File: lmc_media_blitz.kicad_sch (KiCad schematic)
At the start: 30 parts, among them J3 Conn_ARM_JTAG_SWD_10, Q1 BSS138, Q2 BSS138, U1 TPS61222DCK, U2 TLV77333PDBVR, U3 LPC804M101JDH20

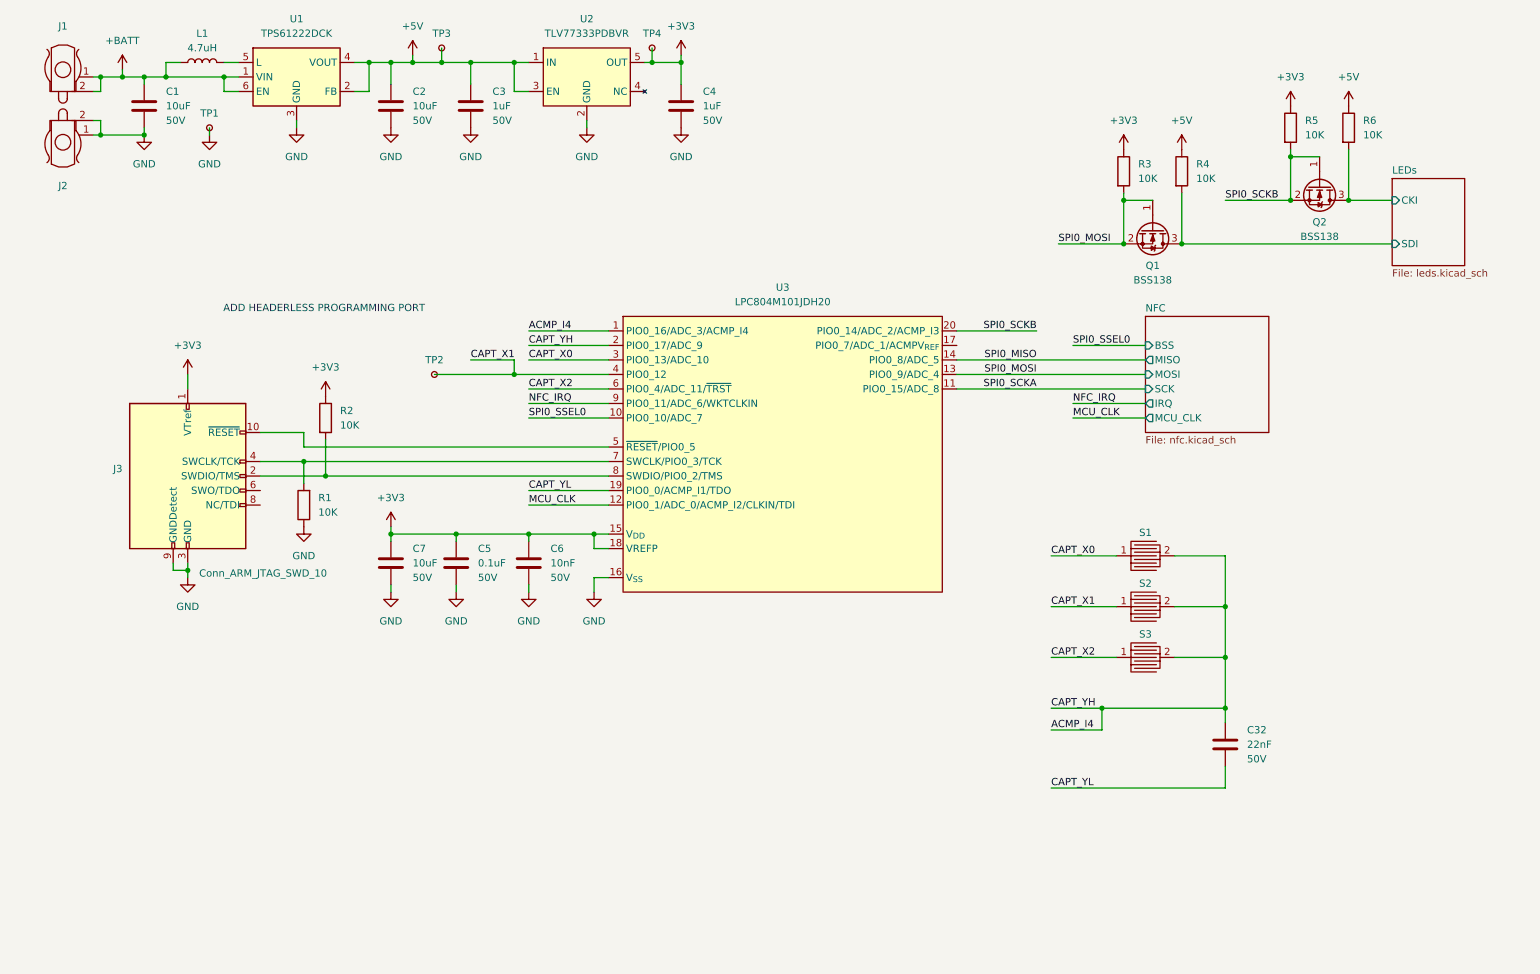
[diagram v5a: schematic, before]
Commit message: Fixed most DRC errors, but need to relayout RFO/RFI
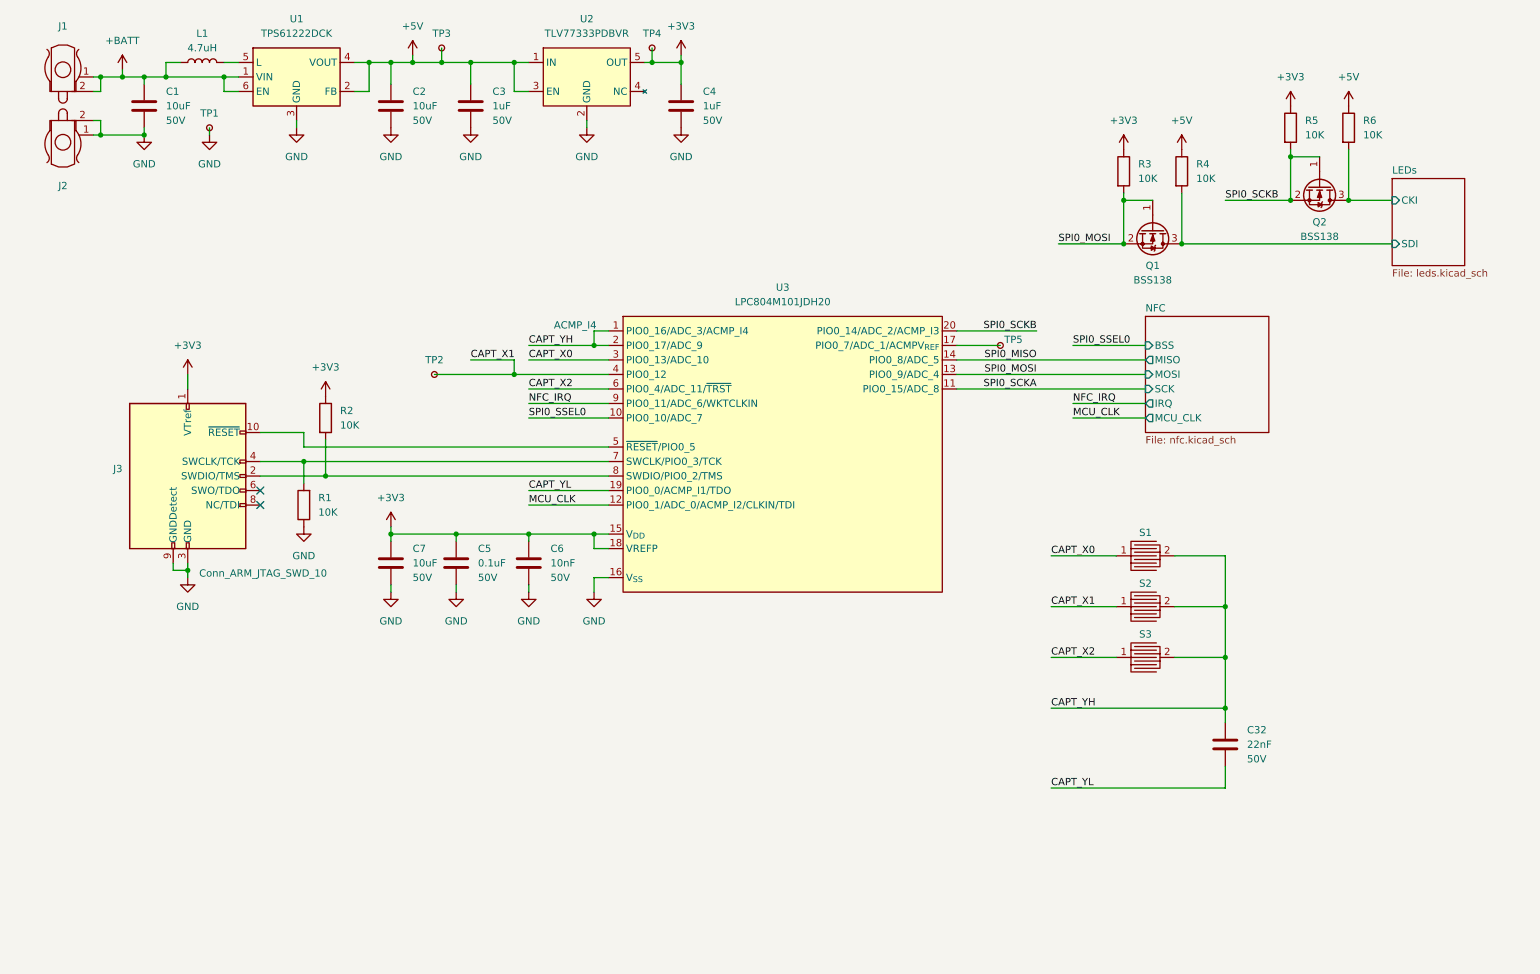
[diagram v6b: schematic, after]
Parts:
- added TP5: TestPoint_Small, TestPoint:TestPoint_Pad_D2.0mm, symbol Connector:TestPoint_Small
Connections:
- net at U3.17 (PIO0_7/ADC_1/ACMPV_{REF}): now also TP5.1
- net ACMP_I4 renamed CAPT_YH
- no-connect marks 0 -> 2
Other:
- note added: "ACMP_I4"
- note removed: "ADD HEADERLESS PROGRAMMING PORT"
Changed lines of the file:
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@@
 	)
 	(junction
-		(at 208.28 52.07)
+		(at 115.57 77.47)
 		(diameter 0)
 		(color 0 0 0 0)
 	)
 	(junction
-		(at 83.82 27.94)
+		(at 208.28 52.07)
 		(diameter 0)
 		(color 0 0 0 0)
 	)
 	(junction
-		(at 237.49 52.07)
+		(at 83.82 27.94)
 		(diameter 0)
 		(color 0 0 0 0)
 	)
 	(junction
-		(at 88.9 27.94)
+		(at 237.49 52.07)
 		(diameter 0)
 		(color 0 0 0 0)
 	)
 	(junction
-		(at 204.47 140.97)
+		(at 88.9 27.94)
 		(diameter 0)
 		(color 0 0 0 0)
@@
 		(color 0 0 0 0)
 	)
+	(no_connect
+		(at 57.15 102.87)
+	)
+	(no_connect
+		(at 57.15 105.41)
+	)
 	(wire
 		(pts
@@
 	(wire
 		(pts
-			(xy 195.58 140.97) (xy 204.47 140.97)
-		)
-		(stroke
-			(width 0)
-			(type default)
-		)
-	)
-	(wire
-		(pts
 			(xy 80.01 27.94) (xy 80.01 31.75)
 		)
@@
 	(wire
 		(pts
-			(xy 104.14 77.47) (xy 118.11 77.47)
+			(xy 104.14 77.47) (xy 115.57 77.47)
 		)
 		(stroke
@@
 	(wire
 		(pts
+			(xy 115.57 74.93) (xy 115.57 77.47)
+		)
+		(stroke
+			(width 0)
+			(type default)
+		)
+	)
+	(wire
+		(pts
 			(xy 91.44 119.38) (xy 91.44 120.65)
 		)
@@
 	(wire
 		(pts
-			(xy 101.6 33.02) (xy 101.6 27.94)
+			(xy 179.07 77.47) (xy 186.69 77.47)
 		)
 		(stroke
@@
 	(wire
 		(pts
-			(xy 104.14 74.93) (xy 118.11 74.93)
+			(xy 101.6 33.02) (xy 101.6 27.94)
 		)
 		(stroke
@@
 	(wire
 		(pts
-			(xy 204.47 144.78) (xy 204.47 140.97)
+			(xy 115.57 77.47) (xy 118.11 77.47)
 		)
 		(stroke
@@
 	(wire
 		(pts
+			(xy 118.11 74.93) (xy 115.57 74.93)
+		)
+		(stroke
+			(width 0)
+			(type default)
+		)
+	)
+	(wire
+		(pts
 			(xy 104.14 85.09) (xy 118.11 85.09)
 		)
@@
 	(wire
 		(pts
-			(xy 195.58 144.78) (xy 204.47 144.78)
-		)
-		(stroke
-			(width 0)
-			(type default)
-		)
-	)
-	(wire
-		(pts
-			(xy 204.47 140.97) (xy 226.06 140.97)
+			(xy 195.58 140.97) (xy 226.06 140.97)
 		)
 		(stroke
@@
 		)
 	)
-	(text "ADD HEADERLESS PROGRAMMING PORT"
+	(text "ACMP_I4"
 		(exclude_from_sim no)
-		(at 68.326 71.12 0)
+		(at 112.268 74.168 0)
 		(effects
 			(font
 				(size 1.27 1.27)
-				(color 255 0 26 1)
 			)
 		)
@@
 		)
 	)
-	(label "ACMP_I4"
-		(at 195.58 144.78 0)
-		(effects
-			(font
-				(size 1.27 1.27)
-			)
-			(justify left bottom)
-		)
-	)
 	(label "CAPT_X2"
 		(at 104.14 85.09 0)
@@
 		)
 	)
-	(label "ACMP_I4"
-		(at 104.14 74.93 0)
-		(effects
-			(font
-				(size 1.27 1.27)
-			)
-			(justify left bottom)
-		)
-	)
 	(label "CAPT_X0"
 		(at 104.14 80.01 0)
@@
 	)
 	(symbol
+		(lib_id "Connector:TestPoint_Small")
+		(at 186.69 77.47 90)
+		(unit 1)
+		(exclude_from_sim no)
+		(in_bom yes)
+		(on_board yes)
+		(dnp no)
+		(property "Reference" "TP5"
+			(at 188.976 76.454 90)
+			(effects
+				(font
+					(size 1.27 1.27)
+				)
+			)
+		)
+		(property "Value" "TestPoint_Small"
+			(at 187.9599 76.2 0)
+			(effects
+				(font
+					(size 1.27 1.27)
+				)
+				(justify left)
+				(hide yes)
+			)
+		)
+		(property "Footprint" "TestPoint:TestPoint_Pad_D2.0mm"
+			(at 186.69 72.39 0)
+			(effects
+				(font
+					(size 1.27 1.27)
+				)
+				(hide yes)
+			)
+		)
+		(property "Datasheet" "~"
+			(at 186.69 72.39 0)
+			(effects
+				(font
+					(size 1.27 1.27)
+				)
+				(hide yes)
+			)
+		)
+		(property "Description" "test point"
+			(at 186.69 77.47 0)
+			(effects
+				(font
+					(size 1.27 1.27)
+				)
+				(hide yes)
+			)
+		)
+		(pin "1"
+		)
+		(instances
+			(project "lmc_media_blitz"
+				(path "/b87eb037-3127-4116-a225-5eb939725614"
+					(reference "TP5")
+					(unit 1)
+				)
+			)
+		)
+	)
+	(symbol
 		(lib_id "Device:R")
 		(at 208.28 46.99 0)
@@
 			)
 		)
-		(property "Datasheet" "https://wmsc.lcsc.com/wmsc/upload/file/pdf/v2/lcsc/2304140030_Taiyo-Yuden-NR3015T4R7M_C87172.pdf"
+		(property "Datasheet" "~"
 			(at 46.99 27.94 0)
 			(effects

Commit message: Added more
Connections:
- net +BATT: now also TP5.1, U3.17 (PIO0_7/ADC_1/ACMPV_{REF})
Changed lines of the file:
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@@
 	)
 	(junction
-		(at 33.02 30.48)
+		(at 35.56 30.48)
 		(diameter 0)
 		(color 0 0 0 0)
@@
 	)
 	(junction
+		(at 31.75 30.48)
+		(diameter 0)
+		(color 0 0 0 0)
+	)
+	(junction
 		(at 208.28 59.69)
 		(diameter 0)
@@
 	(wire
 		(pts
+			(xy 31.75 30.48) (xy 35.56 30.48)
+		)
+		(stroke
+			(width 0)
+			(type default)
+		)
+	)
+	(wire
+		(pts
 			(xy 88.9 25.4) (xy 88.9 27.94)
 		)
@@
 	(wire
 		(pts
+			(xy 36.83 30.48) (xy 40.64 30.48)
+		)
+		(stroke
+			(width 0)
+			(type default)
+		)
+	)
+	(wire
+		(pts
 			(xy 218.44 50.8) (xy 218.44 59.69)
 		)
@@
 	(wire
 		(pts
+			(xy 195.58 71.12) (xy 195.58 77.47)
+		)
+		(stroke
+			(width 0)
+			(type default)
+		)
+	)
+	(wire
+		(pts
 			(xy 195.58 123.19) (xy 207.01 123.19)
 		)
@@
 	(wire
 		(pts
-			(xy 179.07 77.47) (xy 186.69 77.47)
+			(xy 179.07 77.47) (xy 195.58 77.47)
 		)
 		(stroke
@@
 	(wire
 		(pts
-			(xy 33.02 30.48) (xy 33.02 29.21)
+			(xy 31.75 30.48) (xy 31.75 29.21)
 		)
 		(stroke
@@
 	(wire
 		(pts
+			(xy 35.56 27.94) (xy 35.56 30.48)
+		)
+		(stroke
+			(width 0)
+			(type default)
+		)
+	)
+	(wire
+		(pts
 			(xy 115.57 77.47) (xy 118.11 77.47)
 		)
@@
 	(wire
 		(pts
-			(xy 29.21 30.48) (xy 33.02 30.48)
+			(xy 29.21 30.48) (xy 31.75 30.48)
 		)
 		(stroke
@@
 	(wire
 		(pts
-			(xy 36.83 30.48) (xy 33.02 30.48)
+			(xy 36.83 30.48) (xy 35.56 30.48)
 		)
 		(stroke
@@
 	(wire
 		(pts
-			(xy 40.64 30.48) (xy 36.83 30.48)
-		)
-		(stroke
-			(width 0)
-			(type default)
-		)
-	)
-	(wire
-		(pts
 			(xy 44.45 116.84) (xy 44.45 118.11)
 		)
@@
 	(symbol
 		(lib_id "power:+BATT")
-		(at 33.02 29.21 0)
+		(at 31.75 29.21 0)
 		(unit 1)
 		(exclude_from_sim no)
@@
 		(fields_autoplaced yes)
 		(property "Reference" "#PWR04"
-			(at 33.02 33.02 0)
+			(at 31.75 33.02 0)
 			(effects
 				(font
@@
 		)
 		(property "Value" "+BATT"
-			(at 33.02 24.13 0)
+			(at 31.75 24.13 0)
 			(effects
 				(font
@@
 		)
 		(property "Footprint" ""
-			(at 33.02 29.21 0)
+			(at 31.75 29.21 0)
 			(effects
 				(font
@@
 		)
 		(property "Datasheet" ""
-			(at 33.02 29.21 0)
+			(at 31.75 29.21 0)
 			(effects
 				(font
@@
 		)
 		(property "Description" "Power symbol creates a global label with name \"+BATT\""
-			(at 33.02 29.21 0)
+			(at 31.75 29.21 0)
 			(effects
 				(font
@@
 	)
 	(symbol
-		(lib_id "Connector:TestPoint_Small")
-		(at 186.69 77.47 90)
-		(unit 1)
-		(exclude_from_sim no)
-		(in_bom yes)
-		(on_board yes)
-		(dnp no)
-		(property "Reference" "TP5"
-			(at 188.976 76.454 90)
-			(effects
-				(font
-					(size 1.27 1.27)
-				)
-			)
-		)
-		(property "Value" "TestPoint_Small"
-			(at 187.9599 76.2 0)
-			(effects
-				(font
-					(size 1.27 1.27)
-				)
-				(justify left)
-				(hide yes)
-			)
-		)
-		(property "Footprint" "TestPoint:TestPoint_Pad_D2.0mm"
-			(at 186.69 72.39 0)
-			(effects
-				(font
-					(size 1.27 1.27)
-				)
-				(hide yes)
-			)
-		)
-		(property "Datasheet" "~"
-			(at 186.69 72.39 0)
-			(effects
-				(font
-					(size 1.27 1.27)
-				)
-				(hide yes)
-			)
-		)
-		(property "Description" "test point"
-			(at 186.69 77.47 0)
-			(effects
-				(font
-					(size 1.27 1.27)
-				)
-				(hide yes)
-			)
-		)
-		(pin "1"
-		)
-		(instances
-			(project "lmc_media_blitz"
-				(path "/b87eb037-3127-4116-a225-5eb939725614"
-					(reference "TP5")
-					(unit 1)
-				)
-			)
-		)
-	)
-	(symbol
 		(lib_id "Device:R")
 		(at 208.28 46.99 0)
@@
 	)
 	(symbol
+		(lib_id "Connector:TestPoint_Small")
+		(at 35.56 27.94 90)
+		(unit 1)
+		(exclude_from_sim no)
+		(in_bom yes)
+		(on_board yes)
+		(dnp no)
+		(property "Reference" "TP5"
+			(at 37.846 26.924 90)
+			(effects
+				(font
+					(size 1.27 1.27)
+				)
+			)
+		)
+		(property "Value" "TestPoint_Small"
+			(at 36.8299 26.67 0)
+			(effects
+				(font
+					(size 1.27 1.27)
+				)
+				(justify left)
+				(hide yes)
+			)
+		)
+		(property "Footprint" "TestPoint:TestPoint_Pad_D2.0mm"
+			(at 35.56 22.86 0)
+			(effects
+				(font
+					(size 1.27 1.27)
+				)
+				(hide yes)
+			)
+		)
+		(property "Datasheet" "~"
+			(at 35.56 22.86 0)
+			(effects
+				(font
+					(size 1.27 1.27)
+				)
+				(hide yes)
+			)
+		)
+		(property "Description" "test point"
+			(at 35.56 27.94 0)
+			(effects
+				(font
+					(size 1.27 1.27)
+				)
+				(hide yes)
+			)
+		)
+		(pin "1"
+		)
+		(instances
+			(project "lmc_media_blitz"
+				(path "/b87eb037-3127-4116-a225-5eb939725614"
+					(reference "TP5")
+					(unit 1)
+				)
+			)
+		)
+	)
+	(symbol
 		(lib_id "power:GND")
 		(at 44.45 118.11 0)
@@
 					(unit 1)
 				)
+			)
+		)
+	)
+	(symbol
+		(lib_id "power:+BATT")
+		(at 195.58 71.12 0)
+		(unit 1)
+		(exclude_from_sim no)
+		(in_bom yes)
+		(on_board yes)
+		(dnp no)
+		(fields_autoplaced yes)
+		(property "Reference" "#PWR063"
+			(at 195.58 74.93 0)
+			(effects
+				(font
+					(size 1.27 1.27)
+				)
+				(hide yes)
+			)
+		)
+		(property "Value" "+BATT"
+			(at 195.58 66.04 0)
+			(effects
+				(font
+					(size 1.27 1.27)
+				)
+			)
+		)
+		(property "Footprint" ""
+			(at 195.58 71.12 0)
+			(effects
+				(font
+					(size 1.27 1.27)
+				)
+				(hide yes)
+			)
+		)
+		(property "Datasheet" ""
+			(at 195.58 71.12 0)
+			(effects
+				(font
+					(size 1.27 1.27)
+				)
+				(hide yes)
+			)
+		)
+		(property "Description" "Power symbol creates a global label with name \"+BATT\""
+			(at 195.58 71.12 0)
+			(effects
+				(font
+					(size 1.27 1.27)
+				)
+				(hide yes)
+			)
+		)
+		(pin "1"
+		)
+		(instances
+			(project "lmc_media_blitz"
+				(path "/b87eb037-3127-4116-a225-5eb939725614"
+					(reference "#PWR063")
+					(unit 1)
+				)

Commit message: Optimizing components for ordering
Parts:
- C1, C2, C7: LCSC Part # (none) -> C440198
- C3, C4: LCSC Part # (none) -> C28323
- C32: LCSC Part # (none) -> C1729
- C5: LCSC Part # (none) -> C14663
- C6: LCSC Part # (none) -> C57112; MFPN CC0603KRX7R9BB103 -> 0603B103K500NT
- J3: LCSC Part # (none) -> C5296739; MFPN FTSH-105-01-L-DV-007-K -> FTSH-105-01-L-DV-007-K
- L1: LCSC Part # (none) -> C87172
- Q1, Q2: LCSC Part # (none) -> C78284; MFPN (none) -> BSS138
- R1, R2, R3, R4, R5, R6: LCSC Part # (none) -> C17414
- S1, S2, S3, TP1, TP2, TP3, TP4, TP5: now left out of the parts list
- U1: LCSC Part # (none) -> C116461; MFPN (none) -> TPS61222DCK
- U2: LCSC Part # (none) -> C134139; MFPN (none) -> TLV77333PDBVR
- U3: LCSC Part # (none) -> C2056857; MFPN (none) -> LPC804M101JDH20
